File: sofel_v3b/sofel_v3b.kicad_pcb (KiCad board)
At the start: 2 copper layers, 145.4 x 116.3 mm, 107 parts, among them J1 Pimaroni Trackball, J2 4PIN, J3 OLED, SW1 SW_PUSH_LED, SW10 SW_PUSH_LED, SW11 SW_PUSH_LED, SW12 SW_PUSH_LED, SW13 SW_PUSH_LED, SW14 SW_PUSH_LED, SW15 SW_PUSH_LED, SW16 SW_PUSH_LED, SW17 SW_PUSH_LED, SW18 SW_PUSH_LED, SW19 SW_PUSH_LED, SW2 SW_PUSH_LED, SW20 SW_PUSH_LED, SW21 SW_PUSH_LED, SW22 SW_PUSH_LED, SW23 SW_PUSH_LED, SW24 SW_PUSH_LED, SW25 Rotary_Encoder_Switch, SW26 SW_PUSH_LED, SW27 SW_PUSH_LED, SW28 SW_PUSH_LED, SW29 SW_PUSH_LED, SW3 SW_PUSH_LED, SW30 SW_PUSH_LED, SW4 SW_PUSH_LED, SW5 SW_PUSH_LED, SW6 SW_PUSH_LED, SW7 SW_PUSH_LED, SW8 SW_PUSH_LED, SW9 SW_PUSH_LED, U2 SN74AHCT1G125, U3 Pico

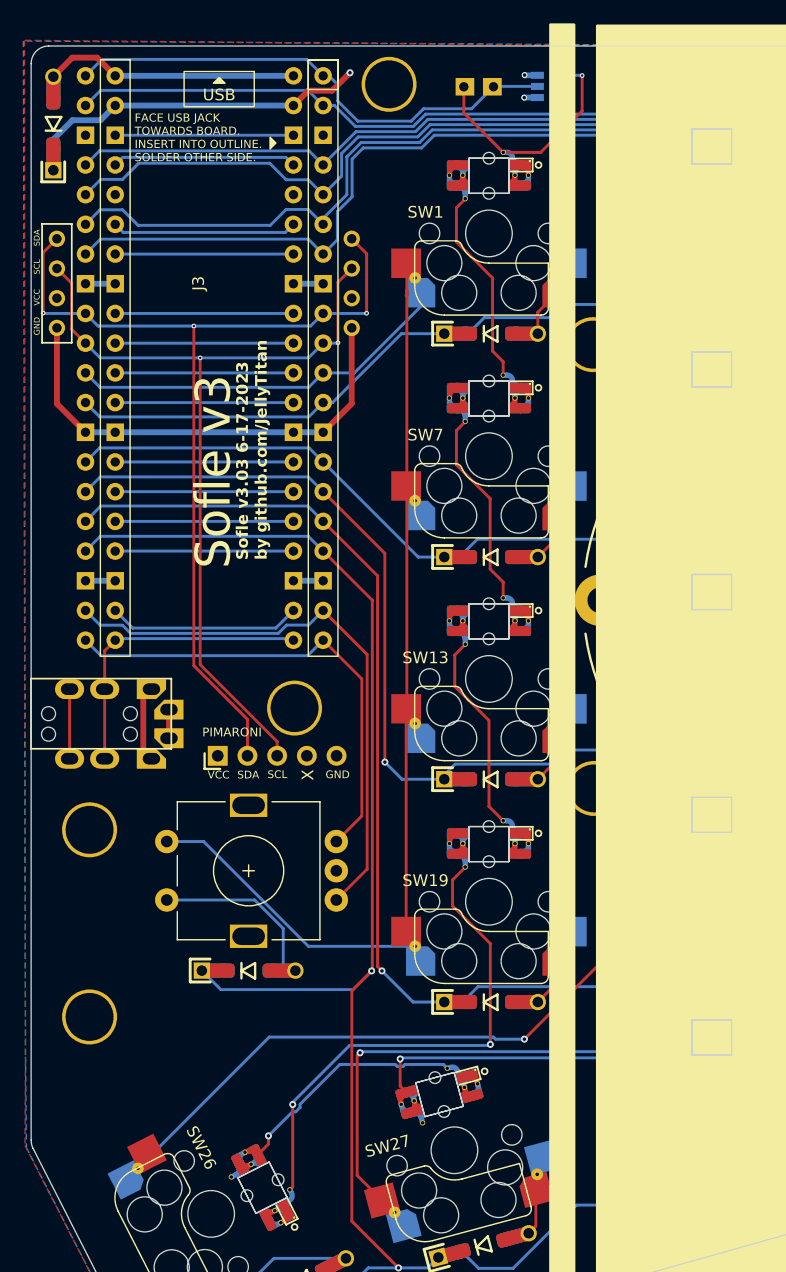
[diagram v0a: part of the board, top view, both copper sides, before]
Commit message: Moved Case holes routing cleanup
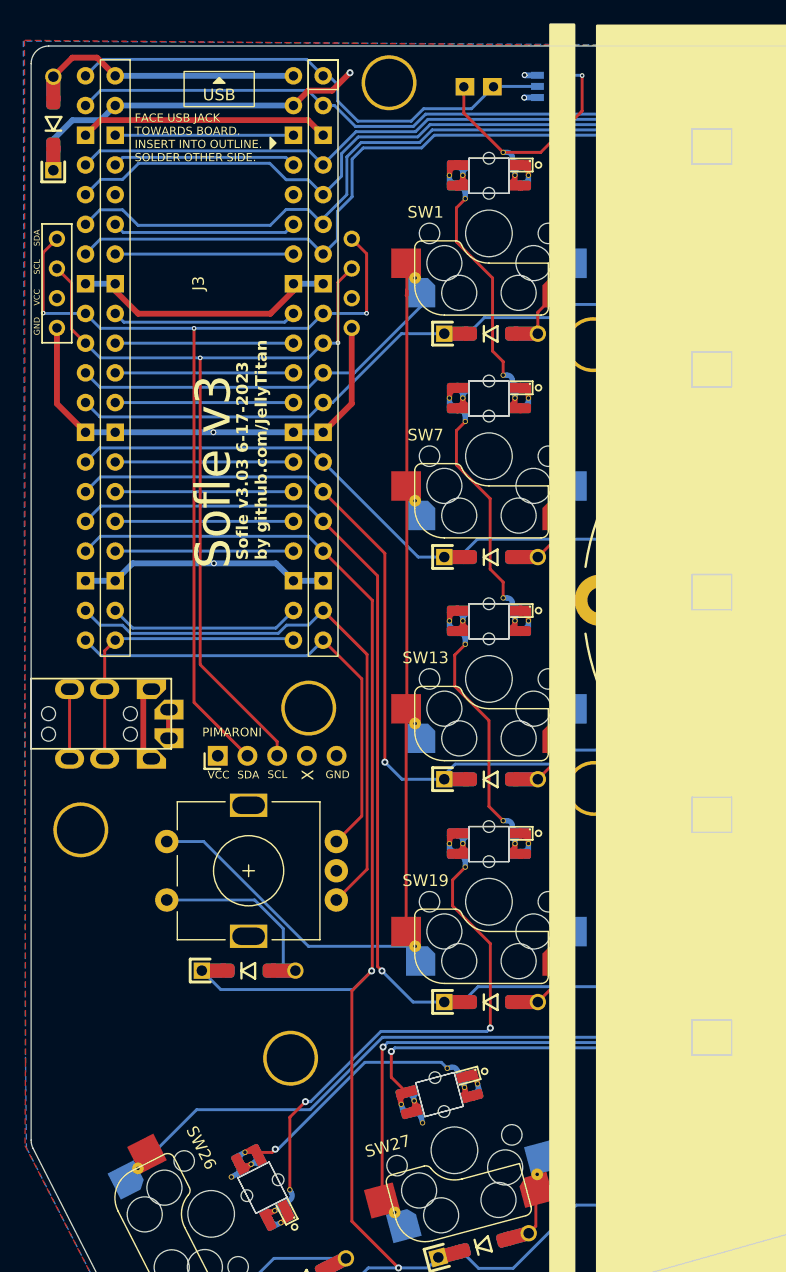
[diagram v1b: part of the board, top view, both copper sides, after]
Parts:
- moved TH8 17.5 mm to (103.6, 120.5)
- moved TH2 1.21 mm to (105.1, 90.6)
- moved TH1 0.75 mm to (85.6, 101.0)
- moved TH7 0.13 mm to (112.0, 37.1)
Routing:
- net GND: track 55.3 -> 111.2 mm, vias 2 -> 4
- net col4: track 175.1 -> 178.9 mm
- net col3: track 203.8 -> 201.1 mm
- net Net-(SW27B-DOUT): track 33.5 -> 35.0 mm
- net Net-(SW19B-DOUT): track 43.5 -> 42.1 mm
- net unconnected-(U3-GPIO27_ADC1-Pad32): track 15.2 -> 15.9 mm
- net Net-(SW26B-DOUT): track 21.2 -> 20.7 mm

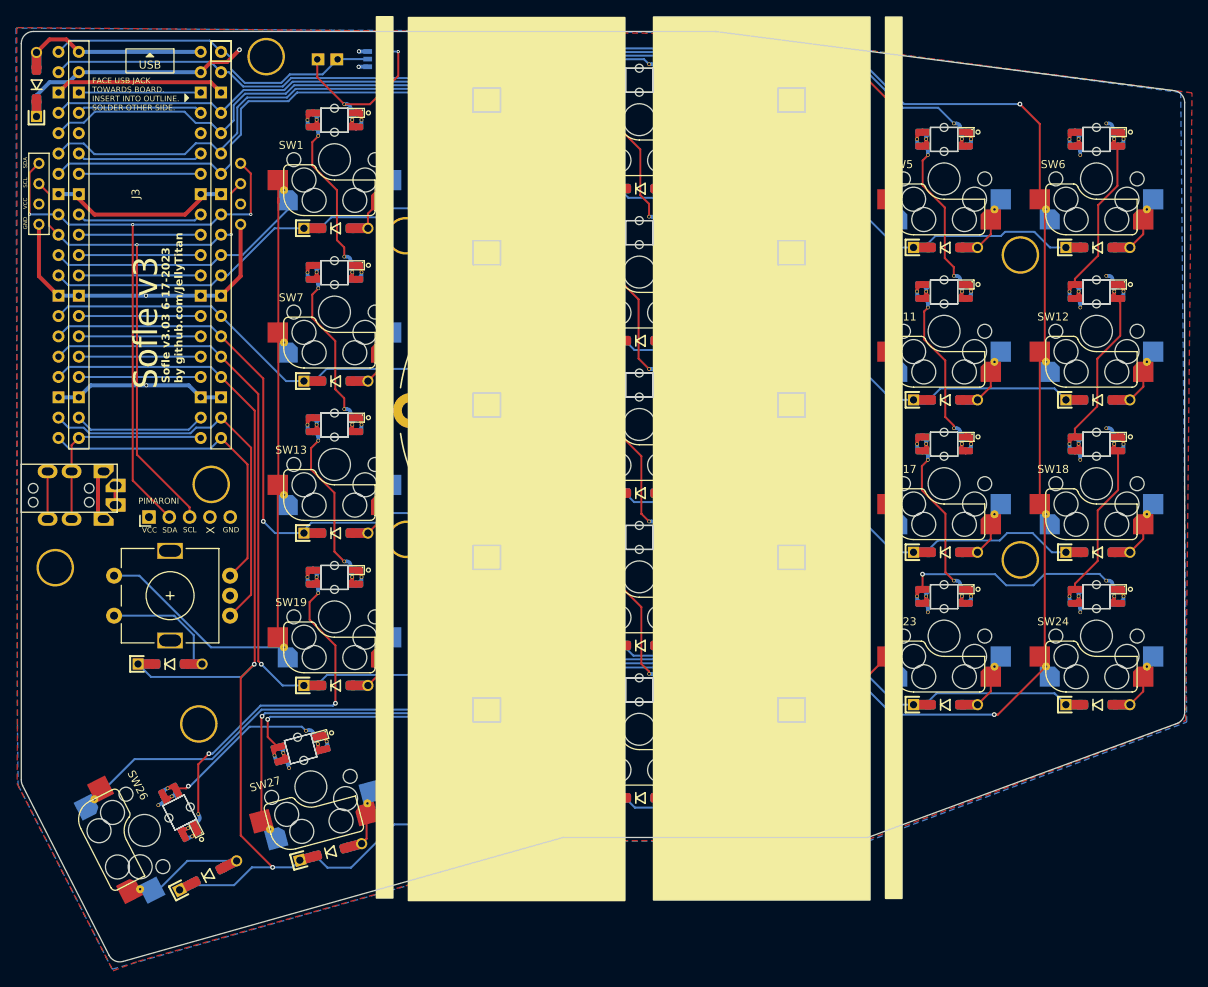
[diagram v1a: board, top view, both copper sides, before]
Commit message: Updated OLED footprint to support multiple models
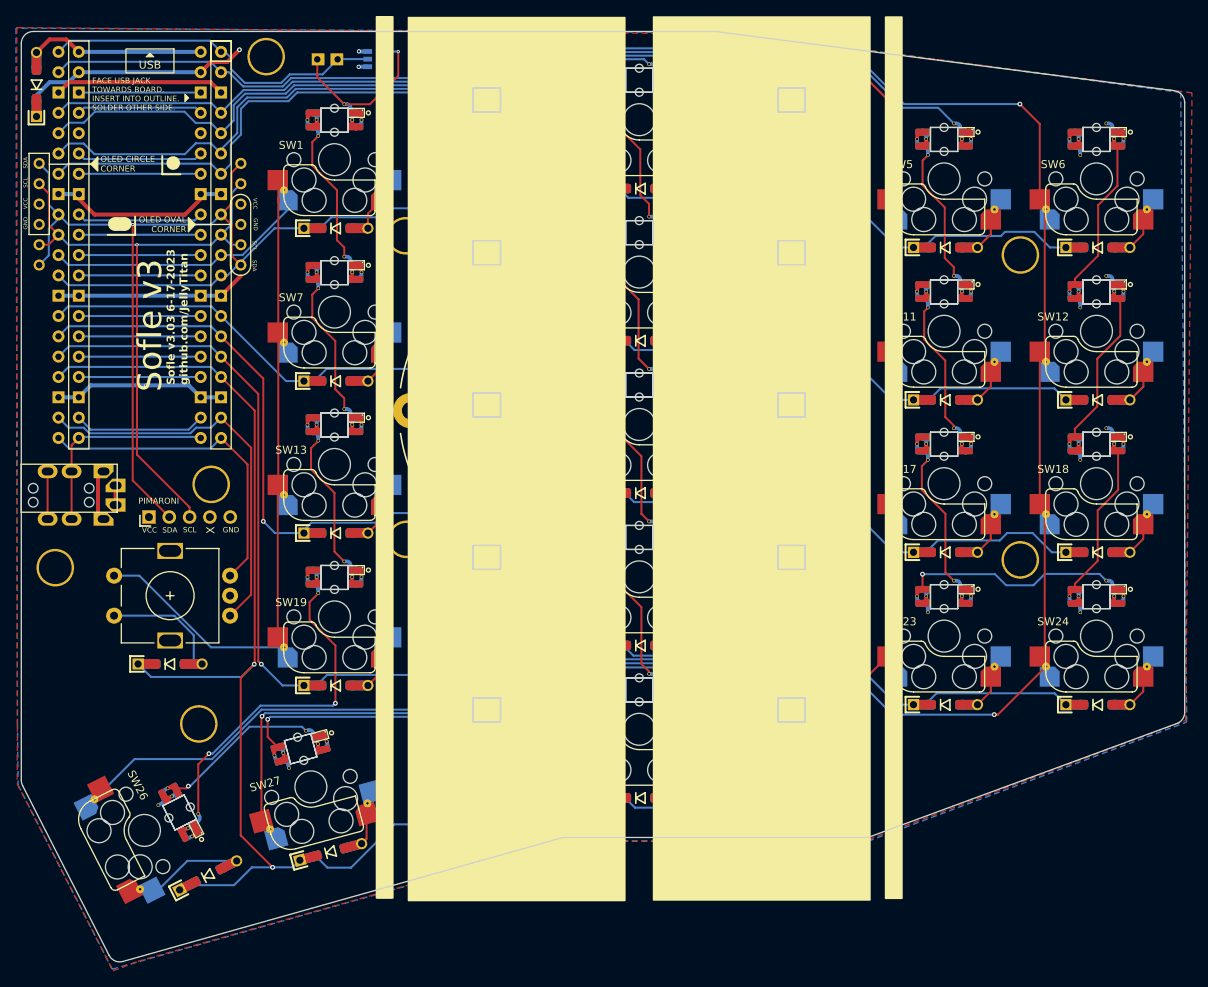
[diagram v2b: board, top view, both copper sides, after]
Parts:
- J3: footprint sofle_v3b:OLED SSD1306 128x64 UNVERIFIED -> sofle_v3b:OLED SSD1306 128x64 UNVERIFIED v2
- turned J3 to -90 degrees
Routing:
- net GND: track 111.2 -> 94.8 mm
- net SDA: track 80.9 -> 89.3 mm, vias 3 -> 1
- net SCL: track 73.6 -> 78.8 mm, vias 2 -> 1
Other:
- board text added: "J3"
- board text added: "OLED CIRCLE CORNER"
- board text added: "OLED OVAL CORNER"
- board text added: "Sofle v3.03 6-17-2023 github.com/JellyTitan"
- board text removed: "Sofle v3.03 6-17-2023 by github.com/JellyTitan"

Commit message: Added full duplex wiring support w/ tx rx firmware crossover
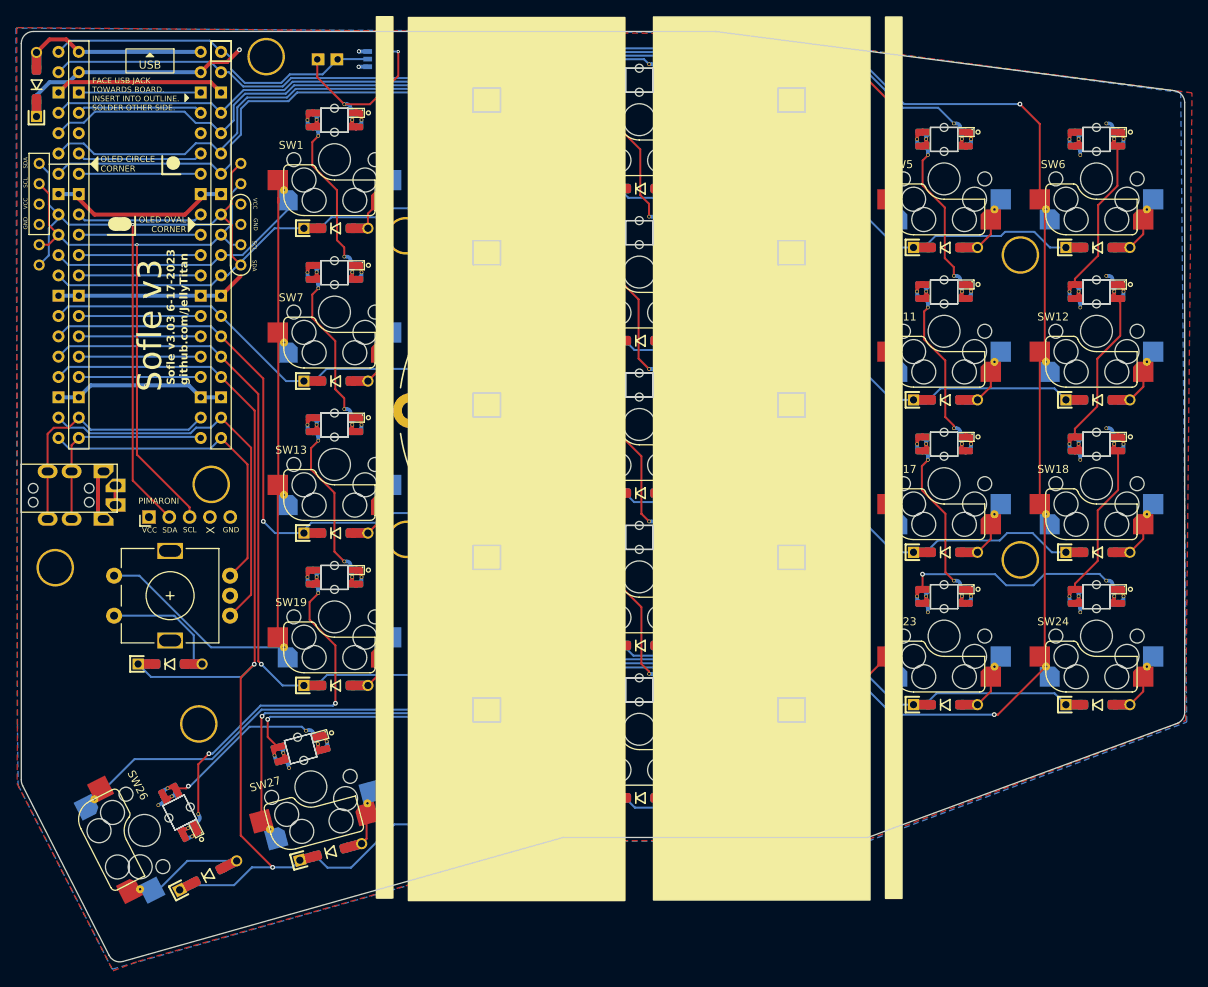
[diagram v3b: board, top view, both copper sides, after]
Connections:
- J2 pad 4: unconnected-(J2-Pad4) -> RX
- U3 pad 22: unconnected-(U3-GPIO17-Pad22) -> RX
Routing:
- net RX: track 0.00 -> 31.9 mm
- net unconnected-(U3-GPIO17-Pad22): track 16.5 -> 0.00 mm
- net unconnected-(J2-Pad4): track 5.95 -> 0.00 mm
